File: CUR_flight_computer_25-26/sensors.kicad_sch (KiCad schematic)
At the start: 8 parts, among them U1 IIS2MDC, U2 LPS22HB

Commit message: Revert "updated sensors"
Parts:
- removed C13: 220n, symbol Device:C_Small
- removed C14: 10u, symbol Device:C_Small
- removed C15: 100n, symbol Device:C_Small
- removed U1: IIS2MDC, ST_IIS2MDC:LGA-12_2X2X0P7_STM, symbol ST_Sensor_IMU:IIS2MDC
- added C2: 4.7u, symbol Device:C_Small
- added U3: LSM6DSV80X, Package_LGA:LGA-14_3x2.5mm_P0.5mm_LayoutBorder3x4y, symbol ST_Sensor_IMU:LSM6DSV80X
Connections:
- net MISO is gone; now on net SENSOR_MISO: U2.5 (SA0)
- net SPC is gone; now on net SENSOR_SPC: U2.2 (SCL)
- net +3V3: now also C1.1, C14.1, C15.1, U2.1 (Vdd_IO), U2.10 (VDD), C2.1
- net GND: now also C14.2, C15.2
- net SENSOR_MOSI: now also U2.4 (SDA)
- no-connect marks 0 -> 4

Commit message: Revert "IMU was not added in main"
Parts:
- removed C14, C15: 100n, symbol Device:C_Small
- removed U3: LSM6DSV80X, Package_LGA:LGA-14_3x2.5mm_P0.5mm_LayoutBorder3x4y, symbol ST_Sensor_IMU:LSM6DSV80X
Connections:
- net GND: now also C2.2, U2.3 (GND), U2.8 (GND), U2.9 (GND)
- no-connect marks 4 -> 0

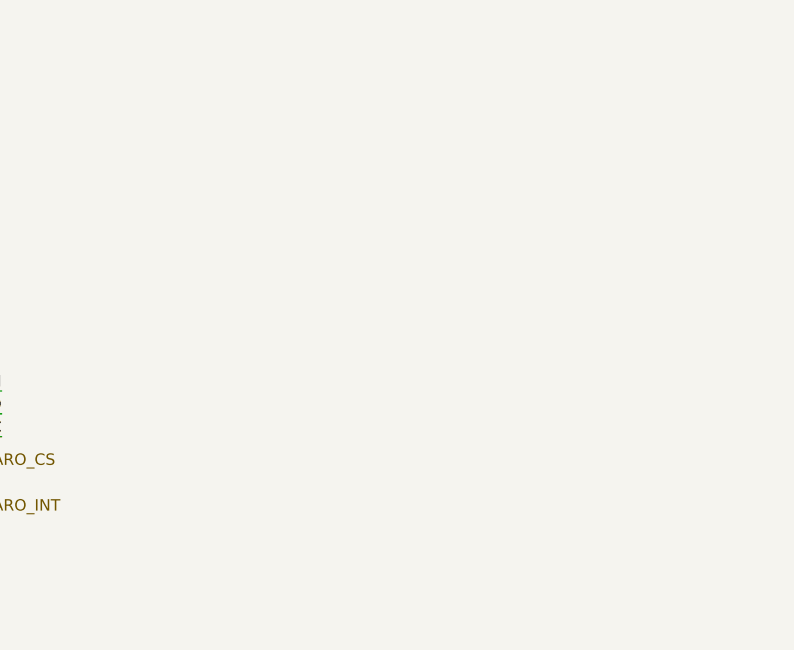
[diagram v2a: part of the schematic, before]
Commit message: Added IMU
- hooked up lsm80
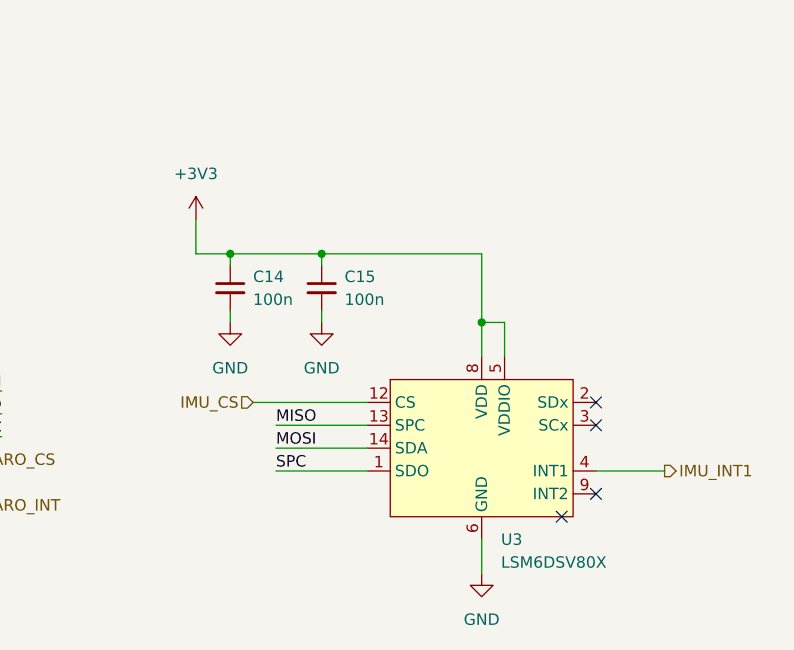
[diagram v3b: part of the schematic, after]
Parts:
- added C14, C15: 100n, symbol Device:C_Small
- added U3: LSM6DSV80X, Package_LGA:LGA-14_3x2.5mm_P0.5mm_LayoutBorder3x4y, symbol ST_Sensor_IMU:LSM6DSV80X
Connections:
- net +3V3: now also C14.1, C15.1, U3.5 (VDDIO), U3.8 (VDD)
- net GND: now also C14.2, C15.2, U3.6 (GND), U3.7 (GND)
- net SENSOR_MISO: now also U3.13 (SCL)
- net SENSOR_MOSI: now also U3.14 (SDA)
- net SENSOR_SPC: now also U3.1 (SDO)
- new net: U3.10 (NC), U3.11 (NC)
- new net IMU_CS: U3.12 (CS)
- new net IMU_INT1: U3.4 (INT1)
- no-connect marks 0 -> 4

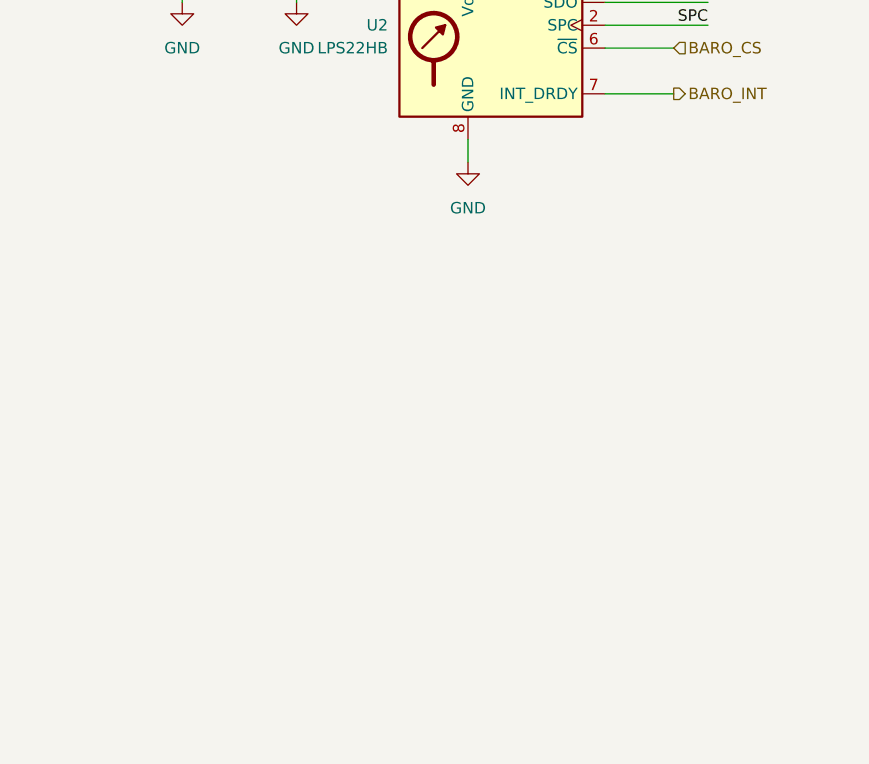
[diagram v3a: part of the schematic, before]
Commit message: fixes
fixed magnitometer
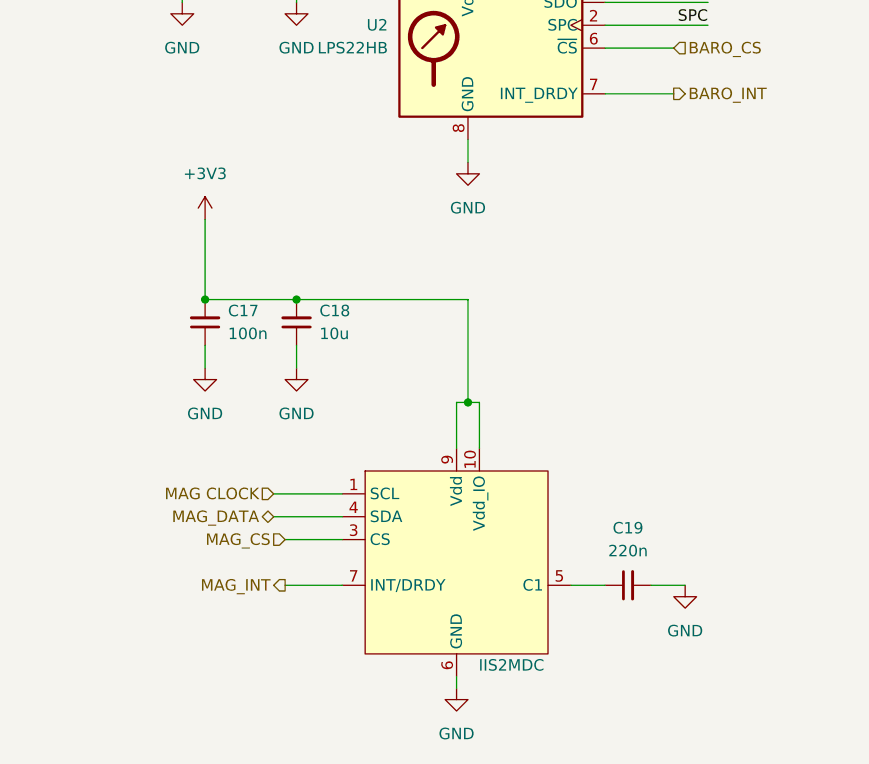
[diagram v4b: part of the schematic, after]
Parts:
- added C17: 100n, symbol Device:C_Small
- added C18: 10u, symbol Device:C_Small
- added C19: 220n, symbol Device:C_Small
- added U6: IIS2MDC, ST_IIS2MDC:LGA-12_2X2X0P7_STM, symbol ST_Sensor_IMU:IIS2MDC
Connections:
- net +3V3: now also C17.2, C18.2, U6.10 (Vdd_IO), U6.9 (Vdd)
- net GND: now also C17.1, C18.1, C19.2, U6.6 (GND), U6.8 (GND)
- new net: C19.1, U6.5 (C1)
- new net: U6.11 (NC), U6.12 (NC), U6.2 (NC)
- new net MAG CLOCK: U6.1 (SCL)
- new net MAG_CS: U6.3 (CS)
- new net MAG_DATA: U6.4 (SDA)
- new net MAG_INT: U6.7 (INT/DRDY)

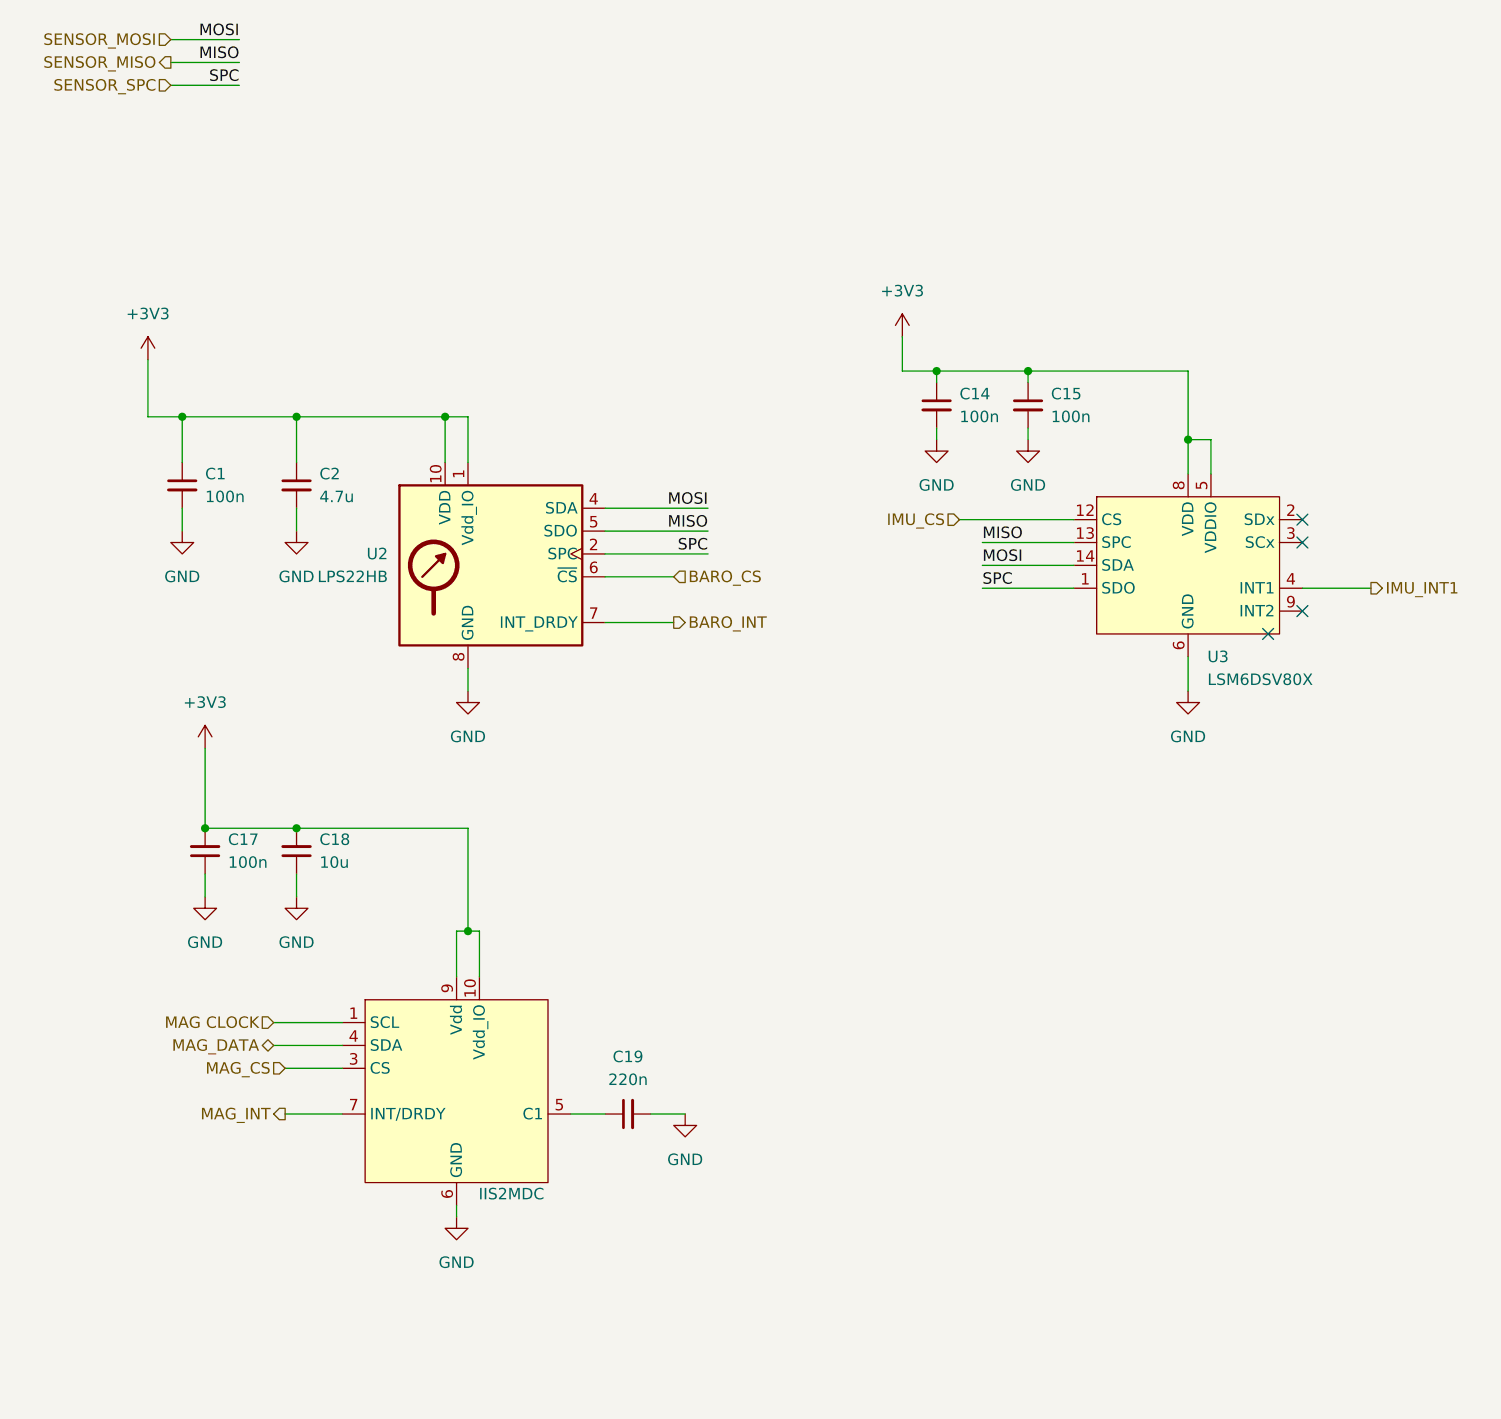
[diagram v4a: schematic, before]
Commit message: Implement RF reference design for LoRA module
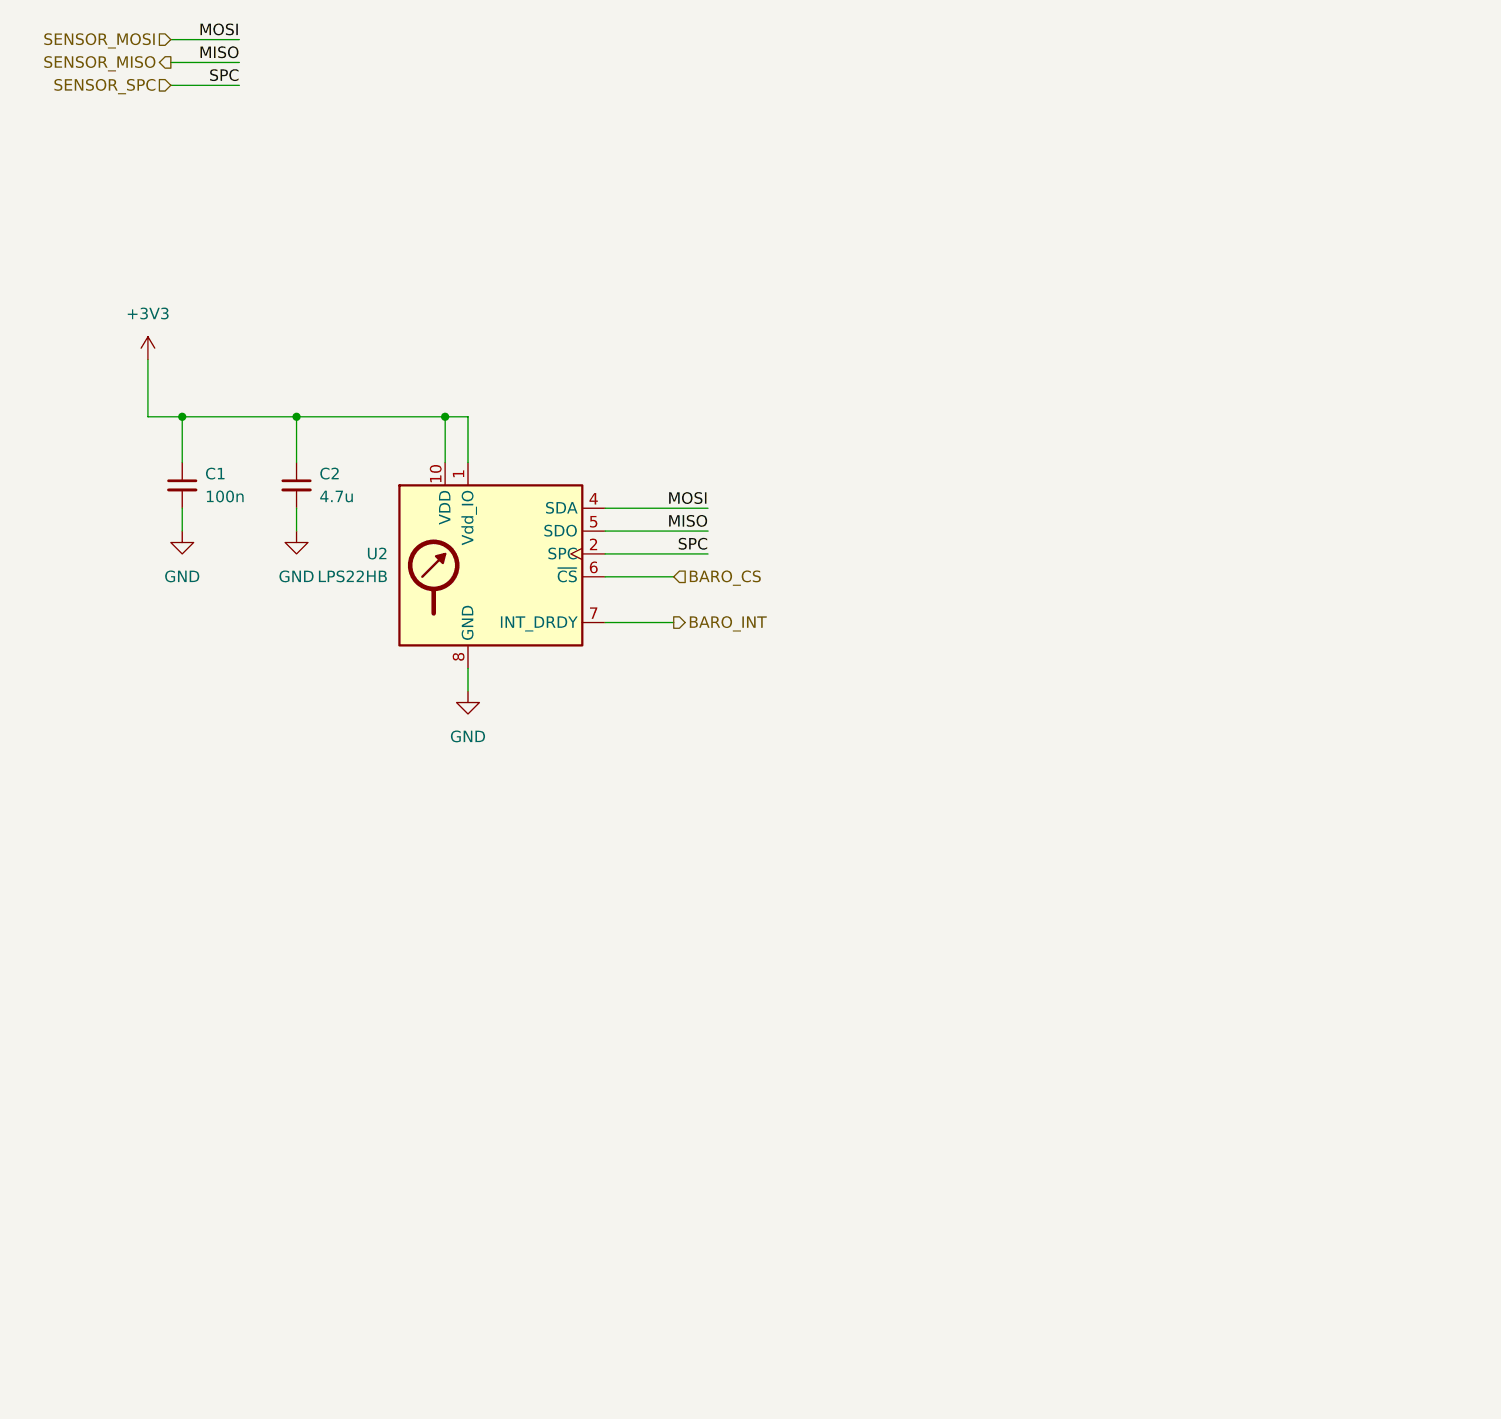
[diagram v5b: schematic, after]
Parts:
- removed C14, C15, C17: 100n, symbol Device:C_Small
- removed C18: 10u, symbol Device:C_Small
- removed C19: 220n, symbol Device:C_Small
- removed U3: LSM6DSV80X, Package_LGA:LGA-14_3x2.5mm_P0.5mm_LayoutBorder3x4y, symbol ST_Sensor_IMU:LSM6DSV80X
- removed U6: IIS2MDC, ST_IIS2MDC:LGA-12_2X2X0P7_STM, symbol ST_Sensor_IMU:IIS2MDC
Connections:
- no-connect marks 4 -> 0

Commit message: Magnitomer
Put In Magnitominer
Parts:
- added C13: 220n, symbol Device:C_Small
- added C14: 10u, symbol Device:C_Small
- added C15: 100n, symbol Device:C_Small
- added U1: IIS2MDC, ST_IIS2MDC:LGA-12_2X2X0P7_STM, symbol ST_Sensor_IMU:IIS2MDC
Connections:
- net +3V3: now also C14.2, C15.2, U1.10 (Vdd_IO), U1.9 (Vdd)
- net GND: now also C13.2, C14.1, C15.1, U1.6 (GND), U1.8 (GND)
- new net: U1.11 (NC), U1.12 (NC), U1.2 (NC)
- new net: C13.1, U1.5 (C1)
- new net MAG CLOCK: U1.1 (SCL)
- new net MAG_CS: U1.3 (CS)
- new net MAG_DATA: U1.4 (SDA)
- new net MAG_INT: U1.7 (INT/DRDY)
